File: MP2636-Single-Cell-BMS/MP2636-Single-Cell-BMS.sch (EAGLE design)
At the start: 36 parts, among them U1 MP2636GR-P

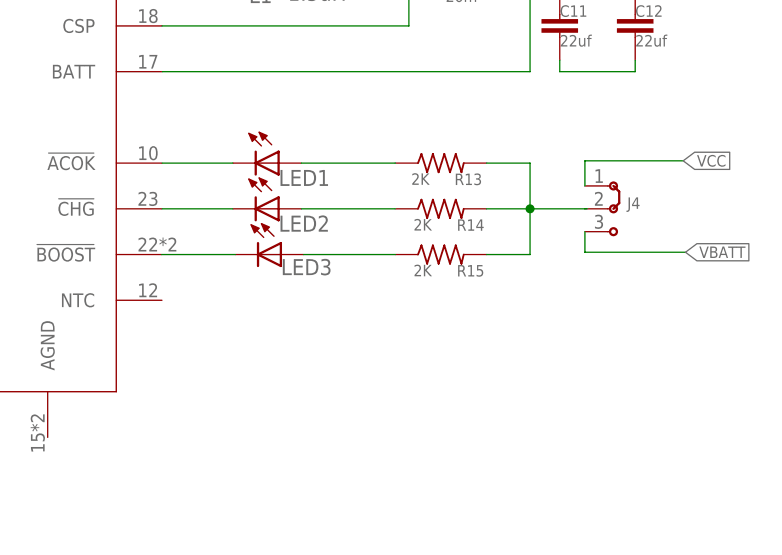
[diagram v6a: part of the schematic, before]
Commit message: NTC added
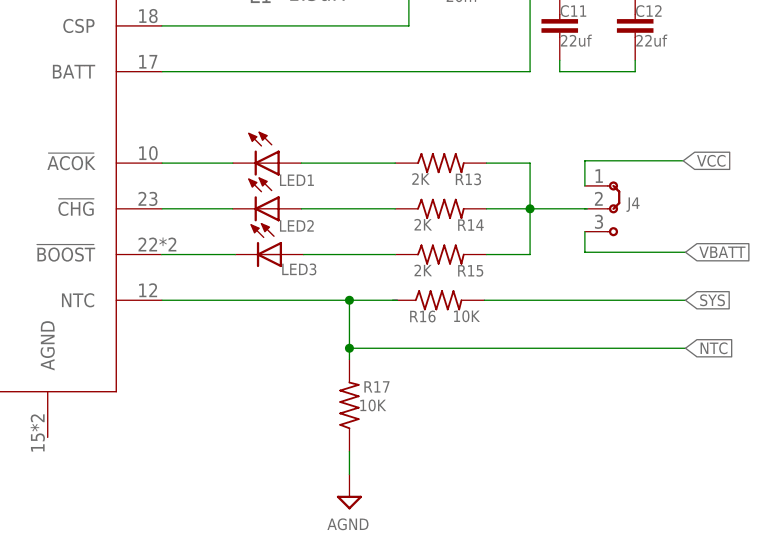
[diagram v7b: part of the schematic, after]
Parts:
- added R16, R17: 10K, Resistor:R-US_CHIP-0805(2012-METRIC)
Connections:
- new net NTC: R16.1, R17.2, U1.NTC
- net AGND: now also R17.1
- net SYS: now also R16.2
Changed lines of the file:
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@@
 <part name="R15" library="Resistor" deviceset="R-US" device="CHIP-0805(2012-METRIC)" package3d_urn="urn:adsk.eagle:package:16378559/2" technology="_" value="2K"/>
 <part name="J4" library="jumper" deviceset="J2" device="X2MM" package3d_urn="urn:adsk.eagle:package:15506/1"/>
+<part name="R16" library="Resistor" deviceset="R-US" device="CHIP-0805(2012-METRIC)" package3d_urn="urn:adsk.eagle:package:16378559/2" technology="_" value="10K"/>
+<part name="R17" library="Resistor" deviceset="R-US" device="CHIP-0805(2012-METRIC)" package3d_urn="urn:adsk.eagle:package:16378559/2" technology="_" value="10K"/>
+<part name="SUPPLY8" library="Power_Symbols" deviceset="AGND" device="" value="AGND"/>
 </parts>
 <sheets>
@@
 </instance>
 <instance part="LED1" gate="G$1" x="172.974" y="96.52" smashed="yes" rot="R270">
-<attribute name="NAME" x="172.974" y="93.98" size="1.778" layer="95"/>
+<attribute name="NAME" x="172.974" y="93.98" size="1.27" layer="95"/>
 <attribute name="VALUE" x="168.402" y="90.805" size="1.778" layer="96"/>
 </instance>
 <instance part="LED2" gate="G$1" x="172.974" y="91.44" smashed="yes" rot="R270">
-<attribute name="NAME" x="172.974" y="88.9" size="1.778" layer="95"/>
+<attribute name="NAME" x="172.974" y="88.9" size="1.27" layer="95"/>
 <attribute name="VALUE" x="168.402" y="85.725" size="1.778" layer="96"/>
 </instance>
 <instance part="LED3" gate="G$1" x="173.228" y="86.36" smashed="yes" rot="R270">
-<attribute name="NAME" x="173.228" y="84.074" size="1.778" layer="95"/>
+<attribute name="NAME" x="173.228" y="84.074" size="1.27" layer="95"/>
 <attribute name="VALUE" x="168.656" y="80.645" size="1.778" layer="96"/>
 </instance>
@@
 <attribute name="NAME" x="211.709" y="91.44" size="1.27" layer="95"/>
 <attribute name="VALUE" x="211.455" y="88.9" size="1.778" layer="96"/>
+</instance>
+<instance part="R16" gate="G$1" x="190.754" y="81.28" smashed="yes">
+<attribute name="NAME" x="188.976" y="79.4766" size="1.27" layer="95" align="center"/>
+<attribute name="VALUE" x="193.802" y="79.502" size="1.27" layer="96" align="center"/>
+</instance>
+<instance part="R17" gate="G$1" x="180.848" y="69.596" smashed="yes" rot="R90">
+<attribute name="NAME" x="183.896" y="71.6534" size="1.27" layer="95" rot="R180" align="center"/>
+<attribute name="VALUE" x="183.388" y="69.596" size="1.27" layer="96" rot="R180" align="center"/>
+</instance>
+<instance part="SUPPLY8" gate="G$1" x="180.848" y="59.436" smashed="yes">
+<attribute name="VALUE" x="180.721" y="55.753" size="1.27" layer="96" align="bottom-center"/>
 </instance>
 </instances>
@@
 <wire x1="152.908" y1="138.938" x2="157.48" y2="138.938" width="0.1524" layer="91"/>
 <wire x1="157.48" y1="138.938" x2="157.48" y2="134.874" width="0.1524" layer="91"/>
+</segment>
+<segment>
+<pinref part="SUPPLY8" gate="G$1" pin="AGND"/>
+<pinref part="R17" gate="G$1" pin="1"/>
+<wire x1="180.848" y1="61.976" x2="180.848" y2="64.516" width="0.1524" layer="91"/>
 </segment>
 </net>
@@
 <label x="217.932" y="142.748" size="1.27" layer="95" xref="yes"/>
 </segment>
+<segment>
+<pinref part="R16" gate="G$1" pin="2"/>
+<wire x1="195.834" y1="81.28" x2="218.186" y2="81.28" width="0.1524" layer="91"/>
+<label x="218.186" y="81.28" size="1.27" layer="95" xref="yes"/>
+</segment>
 </net>
 <net name="FB" class="0">
@@
 </segment>
 </net>
+<net name="NTC" class="0">
+<segment>
+<pinref part="U1" gate="G$1" pin="NTC"/>
+<pinref part="R16" gate="G$1" pin="1"/>
+<wire x1="160.02" y1="81.28" x2="180.848" y2="81.28" width="0.1524" layer="91"/>
+<wire x1="180.848" y1="81.28" x2="185.674" y2="81.28" width="0.1524" layer="91"/>
+<wire x1="186.182" y1="81.28" x2="185.674" y2="81.28" width="0.1524" layer="91"/>
+<pinref part="R17" gate="G$1" pin="2"/>
+<wire x1="180.848" y1="74.676" x2="180.848" y2="75.946" width="0.1524" layer="91"/>
+<junction x="180.848" y="81.28"/>
+<wire x1="180.848" y1="75.946" x2="180.848" y2="81.28" width="0.1524" layer="91"/>
+<wire x1="180.848" y1="75.946" x2="218.186" y2="75.946" width="0.1524" layer="91"/>
+<junction x="180.848" y="75.946"/>
+<label x="218.186" y="75.946" size="1.27" layer="95" xref="yes"/>
+</segment>
+</net>

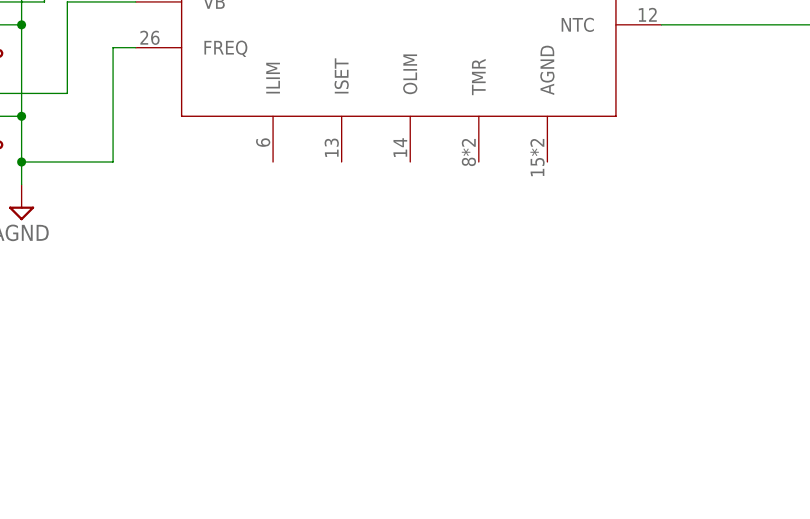
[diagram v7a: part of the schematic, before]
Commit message: Current limit circuit is added
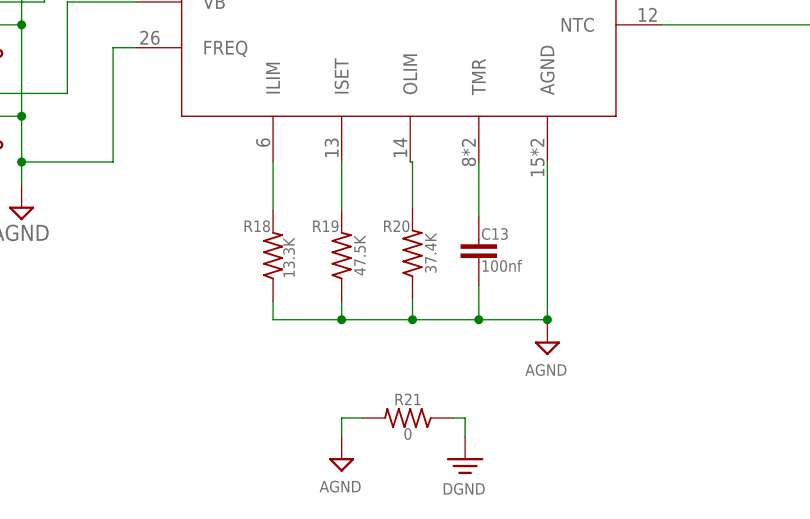
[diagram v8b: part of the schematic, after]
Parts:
- added C13: 100nf, Capacitor:C_CHIP-0805(2012-METRIC)
- added R18: 13.3K, Resistor:R-US_CHIP-0805(2012-METRIC)
- added R19: 47.5K, Resistor:R-US_CHIP-0805(2012-METRIC)
- added R20: 37.4K, Resistor:R-US_CHIP-0805(2012-METRIC)
- added R21: 0, Resistor:R-US_CHIP-0805(2012-METRIC)
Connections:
- new net N$20: R18.2, U1.ILIM
- new net N$21: R19.2, U1.ISET
- new net N$22: R20.2, U1.OLIM
- new net N$23: C13.1, U1.TMR
- net AGND: now also C13.2, R18.1, R19.1, R20.1, R21.2, U1.AGND
- net DGND: now also R21.1
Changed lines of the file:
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@@
 <part name="R17" library="Resistor" deviceset="R-US" device="CHIP-0805(2012-METRIC)" package3d_urn="urn:adsk.eagle:package:16378559/2" technology="_" value="10K"/>
 <part name="SUPPLY8" library="Power_Symbols" deviceset="AGND" device="" value="AGND"/>
+<part name="R18" library="Resistor" deviceset="R-US" device="CHIP-0805(2012-METRIC)" package3d_urn="urn:adsk.eagle:package:16378559/2" technology="_" value="13.3K"/>
+<part name="R19" library="Resistor" deviceset="R-US" device="CHIP-0805(2012-METRIC)" package3d_urn="urn:adsk.eagle:package:16378559/2" technology="_" value="47.5K"/>
+<part name="R20" library="Resistor" deviceset="R-US" device="CHIP-0805(2012-METRIC)" package3d_urn="urn:adsk.eagle:package:16378559/2" technology="_" value="37.4K"/>
+<part name="C13" library="Capacitor" deviceset="C" device="CHIP-0805(2012-METRIC)" package3d_urn="urn:adsk.eagle:package:16290897/2" technology="_" value="100nf"/>
+<part name="SUPPLY9" library="Power_Symbols" deviceset="AGND" device="" value="AGND"/>
+<part name="SUPPLY10" library="Power_Symbols" deviceset="AGND" device="" value="AGND"/>
+<part name="SUPPLY11" library="Power_Symbols" deviceset="DGND-EARTH" device="" value="DGND"/>
+<part name="R21" library="Resistor" deviceset="R-US" device="CHIP-0805(2012-METRIC)" package3d_urn="urn:adsk.eagle:package:16378559/2" technology="_" value="0"/>
 </parts>
 <sheets>
@@
 <instance part="SUPPLY8" gate="G$1" x="180.848" y="59.436" smashed="yes">
 <attribute name="VALUE" x="180.721" y="55.753" size="1.27" layer="96" align="bottom-center"/>
+</instance>
+<instance part="R18" gate="G$1" x="116.84" y="55.626" smashed="yes" rot="R90">
+<attribute name="NAME" x="115.062" y="58.9026" size="1.27" layer="95" align="center"/>
+<attribute name="VALUE" x="118.618" y="55.372" size="1.27" layer="96" rot="R90" align="center"/>
+</instance>
+<instance part="R19" gate="G$1" x="124.46" y="55.626" smashed="yes" rot="R90">
+<attribute name="NAME" x="122.682" y="58.9026" size="1.27" layer="95" align="center"/>
+<attribute name="VALUE" x="126.492" y="55.626" size="1.27" layer="96" rot="R90" align="center"/>
+</instance>
+<instance part="R20" gate="G$1" x="132.334" y="55.88" smashed="yes" rot="R90">
+<attribute name="NAME" x="130.556" y="58.9026" size="1.27" layer="95" align="center"/>
+<attribute name="VALUE" x="134.366" y="55.88" size="1.27" layer="96" rot="R90" align="center"/>
+</instance>
+<instance part="C13" gate="G$1" x="139.7" y="57.404" smashed="yes">
+<attribute name="NAME" x="139.954" y="57.404" size="1.27" layer="95"/>
+<attribute name="VALUE" x="139.954" y="53.848" size="1.27" layer="96"/>
+</instance>
+<instance part="SUPPLY9" gate="G$1" x="147.32" y="45.974" smashed="yes">
+<attribute name="VALUE" x="147.193" y="42.291" size="1.27" layer="96" align="bottom-center"/>
+</instance>
+<instance part="SUPPLY10" gate="G$1" x="124.46" y="33.02" smashed="yes">
+<attribute name="VALUE" x="124.333" y="29.337" size="1.27" layer="96" align="bottom-center"/>
+</instance>
+<instance part="SUPPLY11" gate="G$1" x="138.176" y="33.02" smashed="yes">
+<attribute name="VALUE" x="138.049" y="29.083" size="1.27" layer="96" align="bottom-center"/>
+</instance>
+<instance part="R21" gate="G$1" x="131.826" y="37.592" smashed="yes" rot="R180">
+<attribute name="NAME" x="131.826" y="39.6494" size="1.27" layer="95" rot="R180" align="center"/>
+<attribute name="VALUE" x="131.826" y="35.814" size="1.27" layer="96" rot="R180" align="center"/>
 </instance>
 </instances>
@@
 <wire x1="210.82" y1="137.668" x2="210.82" y2="136.652" width="0.1524" layer="91"/>
 </segment>
+<segment>
+<pinref part="R21" gate="G$1" pin="1"/>
+<pinref part="SUPPLY11" gate="G$1" pin="DGND"/>
+<wire x1="136.906" y1="37.592" x2="138.176" y2="37.592" width="0.1524" layer="91"/>
+<wire x1="138.176" y1="37.592" x2="138.176" y2="35.56" width="0.1524" layer="91"/>
+</segment>
 </net>
 <net name="N$2" class="0">
@@
 <pinref part="R17" gate="G$1" pin="1"/>
 <wire x1="180.848" y1="61.976" x2="180.848" y2="64.516" width="0.1524" layer="91"/>
+</segment>
+<segment>
+<pinref part="U1" gate="G$1" pin="AGND"/>
+<pinref part="SUPPLY9" gate="G$1" pin="AGND"/>
+<wire x1="147.32" y1="66.04" x2="147.32" y2="48.514" width="0.1524" layer="91"/>
+<wire x1="139.7" y1="48.514" x2="147.32" y2="48.514" width="0.1524" layer="91"/>
+<junction x="147.32" y="48.514"/>
+<pinref part="R18" gate="G$1" pin="1"/>
+<wire x1="116.84" y1="50.546" x2="116.84" y2="48.514" width="0.1524" layer="91"/>
+<wire x1="116.84" y1="48.514" x2="124.46" y2="48.514" width="0.1524" layer="91"/>
+<pinref part="R19" gate="G$1" pin="1"/>
+<wire x1="124.46" y1="48.514" x2="124.46" y2="50.546" width="0.1524" layer="91"/>
+<wire x1="124.46" y1="48.514" x2="132.334" y2="48.514" width="0.1524" layer="91"/>
+<junction x="124.46" y="48.514"/>
+<pinref part="R20" gate="G$1" pin="1"/>
+<wire x1="132.334" y1="48.514" x2="132.334" y2="50.8" width="0.1524" layer="91"/>
+<wire x1="132.334" y1="48.514" x2="139.7" y2="48.514" width="0.1524" layer="91"/>
+<junction x="132.334" y="48.514"/>
+<pinref part="C13" gate="G$1" pin="2"/>
+<wire x1="139.7" y1="48.514" x2="139.7" y2="52.324" width="0.1524" layer="91"/>
+<junction x="139.7" y="48.514"/>
+</segment>
+<segment>
+<pinref part="SUPPLY10" gate="G$1" pin="AGND"/>
+<wire x1="124.46" y1="35.56" x2="124.46" y2="37.592" width="0.1524" layer="91"/>
+<wire x1="124.46" y1="37.592" x2="126.746" y2="37.592" width="0.1524" layer="91"/>
+<pinref part="R21" gate="G$1" pin="2"/>
 </segment>
 </net>
@@
 </segment>
 </net>
+<net name="N$20" class="0">
+<segment>
+<pinref part="U1" gate="G$1" pin="ILIM"/>
+<pinref part="R18" gate="G$1" pin="2"/>
+<wire x1="116.84" y1="66.04" x2="116.84" y2="60.706" width="0.1524" layer="91"/>
+</segment>
+</net>
+<net name="N$21" class="0">
+<segment>
+<pinref part="R19" gate="G$1" pin="2"/>
+<pinref part="U1" gate="G$1" pin="ISET"/>
+<wire x1="124.46" y1="60.706" x2="124.46" y2="66.04" width="0.1524" layer="91"/>
+</segment>
+</net>
+<net name="N$22" class="0">
+<segment>
+<pinref part="U1" gate="G$1" pin="OLIM"/>
+<pinref part="R20" gate="G$1" pin="2"/>
+<wire x1="132.08" y1="66.04" x2="132.334" y2="66.04" width="0.1524" layer="91"/>
+<wire x1="132.334" y1="66.04" x2="132.334" y2="60.96" width="0.1524" layer="91"/>
+</segment>
+</net>
+<net name="N$23" class="0">
+<segment>
+<pinref part="U1" gate="G$1" pin="TMR"/>
+<pinref part="C13" gate="G$1" pin="1"/>
+<wire x1="139.7" y1="66.04" x2="139.7" y2="59.944" width="0.1524" layer="91"/>
+</segment>
+</net>
